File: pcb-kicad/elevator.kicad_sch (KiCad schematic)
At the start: 145 parts, among them SW1 MX-with-LED, SW10 MX-with-LED, SW11 MX-with-LED, SW12 MX-with-LED, SW13 MX-with-LED, SW14 MX-with-LED, SW15 MX-with-LED, SW16 MX-with-LED, SW17 MX-with-LED, SW18 MX-with-LED, SW19 MX-with-LED, SW2 MX-with-LED, SW20 MX-with-LED, SW21 MX-with-LED, SW22 MX-with-LED, SW23 MX-with-LED, SW24 MX-with-LED, SW25 MX-with-LED, SW26 MX-with-LED, SW27 MX-with-LED, SW28 MX-with-LED, SW29 MX-with-LED, SW3 MX-with-LED, SW30 MX-with-LED, SW31 MX-with-LED, SW32 MX-with-LED, SW33 MX-with-LED, SW34 MX-with-LED, SW35 MX-with-LED, SW36 MX-with-LED, SW37 MX-with-LED, SW38 MX-with-LED, SW39 MX-with-LED, SW4 MX-with-LED, SW40 MX-with-LED, SW41 MX-with-LED, SW42 MX-with-LED, SW43 MX-with-LED, SW44 MX-with-LED, SW45 MX-with-LED, SW46 MX-with-LED, SW47 MX-with-LED, SW48 MX-with-LED, SW5 MX-with-LED, SW6 MX-with-LED, SW7 MX-with-LED, SW8 MX-with-LED, SW9 MX-with-LED, U1 Frood

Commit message: Update schematic
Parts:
- added Q1: AO3416, Package_TO_SOT_SMD:SOT-23, symbol Transistor_FET:AO3400A
- added R49: R_LED_PWM, symbol Device:R_Small
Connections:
- net COL0: now also U1.26 (GPIO29)
- net COL1: now also U1.25 (GPIO28)
- net COL2: now also U1.24 (GPIO27)
- net COL3: now also U1.23 (GPIO26)
- net COL4: now also U1.22 (GPIO22)
- net COL5: now also U1.21 (GPIO20)
- net GND: now also U1.4 (GND), U1.5 (GND), Q1.2 (S)
- net LED_D: now also Q1.3 (D)
- net ROW0: now also U1.2 (GPIO0)
- net ROW1: now also U1.3 (GPIO1)
- net ROW2: now also U1.6 (GPIO2)
- net ROW3: now also U1.7 (GPIO3)
- net ROW4: now also U1.8 (GPIO4)
- net ROW5: now also U1.9 (GPIO5)
- net ROW6: now also U1.10 (GPIO6)
- net ROW7: now also U1.11 (GPIO7)
- net LED_PWM: now reaches U1.19 (GPIO21)
- net LED_PWM: now also R49.2
- new net: Q1.1 (G), R49.1
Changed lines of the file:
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@@
     (effects (font (size 1.27 1.27)) (justify right bottom))
   )
+  (label "LED_D" (at 58.42 33.02 180) (fields_autoplaced)
+    (effects (font (size 1.27 1.27)) (justify right bottom))
+  )
   (label "ROW6" (at 170.18 129.54 180) (fields_autoplaced)
     (effects (font (size 1.27 1.27)) (justify right bottom))
   )
+  (label "COL2" (at 104.14 100.33 0) (fields_autoplaced)
+    (effects (font (size 1.27 1.27)) (justify left bottom))
+  )
   (label "VCC" (at 350.52 121.92 180) (fields_autoplaced)
     (effects (font (size 1.27 1.27)) (justify right bottom))
   )
+  (label "LED_PWM" (at 63.5 45.72 270) (fields_autoplaced)
+    (effects (font (size 1.27 1.27)) (justify right bottom))
+  )
+  (label "COL5" (at 104.14 107.95 0) (fields_autoplaced)
+    (effects (font (size 1.27 1.27)) (justify left bottom))
+  )
   (label "VCC" (at 236.22 97.79 180) (fields_autoplaced)
     (effects (font (size 1.27 1.27)) (justify right bottom))
@@
     (effects (font (size 1.27 1.27)) (justify right bottom))
   )
+  (label "ROW1" (at 63.5 87.63 180) (fields_autoplaced)
+    (effects (font (size 1.27 1.27)) (justify right bottom))
+  )
   (label "VCC" (at 179.07 97.79 180) (fields_autoplaced)
     (effects (font (size 1.27 1.27)) (justify right bottom))
@@
     (effects (font (size 1.27 1.27)) (justify left bottom))
   )
+  (label "COL0" (at 104.14 95.25 0) (fields_autoplaced)
+    (effects (font (size 1.27 1.27)) (justify left bottom))
+  )
   (label "LED_D" (at 360.68 55.88 180) (fields_autoplaced)
     (effects (font (size 1.27 1.27)) (justify right bottom))
@@
     (effects (font (size 1.27 1.27)) (justify left bottom))
   )
+  (label "ROW6" (at 63.5 105.41 180) (fields_autoplaced)
+    (effects (font (size 1.27 1.27)) (justify right bottom))
+  )
   (label "VCC" (at 388.62 50.8 180) (fields_autoplaced)
     (effects (font (size 1.27 1.27)) (justify right bottom))
@@
     (effects (font (size 1.27 1.27)) (justify right bottom))
   )
+  (label "GND" (at 68.58 33.02 0) (fields_autoplaced)
+    (effects (font (size 1.27 1.27)) (justify left bottom))
+  )
+  (label "GND" (at 63.5 90.17 180) (fields_autoplaced)
+    (effects (font (size 1.27 1.27)) (justify right bottom))
+  )
   (label "VCC" (at 255.27 50.8 180) (fields_autoplaced)
     (effects (font (size 1.27 1.27)) (justify right bottom))
@@
     (effects (font (size 1.27 1.27)) (justify right bottom))
   )
+  (label "ROW4" (at 63.5 100.33 180) (fields_autoplaced)
+    (effects (font (size 1.27 1.27)) (justify right bottom))
+  )
   (label "VCC" (at 236.22 74.93 180) (fields_autoplaced)
     (effects (font (size 1.27 1.27)) (justify right bottom))
   )
+  (label "COL3" (at 104.14 102.87 0) (fields_autoplaced)
+    (effects (font (size 1.27 1.27)) (justify left bottom))
+  )
   (label "LED_D" (at 398.78 102.87 180) (fields_autoplaced)
     (effects (font (size 1.27 1.27)) (justify right bottom))
   )
+  (label "ROW5" (at 63.5 102.87 180) (fields_autoplaced)
+    (effects (font (size 1.27 1.27)) (justify right bottom))
+  )
   (label "LED_D" (at 303.53 127 180) (fields_autoplaced)
     (effects (font (size 1.27 1.27)) (justify right bottom))
@@
     (effects (font (size 1.27 1.27)) (justify right bottom))
   )
+  (label "ROW7" (at 63.5 107.95 180) (fields_autoplaced)
+    (effects (font (size 1.27 1.27)) (justify right bottom))
+  )
   (label "VCC" (at 350.52 50.8 180) (fields_autoplaced)
     (effects (font (size 1.27 1.27)) (justify right bottom))
@@
     (effects (font (size 1.27 1.27)) (justify right bottom))
   )
+  (label "ROW0" (at 63.5 85.09 180) (fields_autoplaced)
+    (effects (font (size 1.27 1.27)) (justify right bottom))
+  )
   (label "LED_D" (at 246.38 80.01 180) (fields_autoplaced)
     (effects (font (size 1.27 1.27)) (justify right bottom))
@@
     (effects (font (size 1.27 1.27)) (justify left bottom))
   )
+  (label "ROW2" (at 63.5 95.25 180) (fields_autoplaced)
+    (effects (font (size 1.27 1.27)) (justify right bottom))
+  )
   (label "LED_D" (at 227.33 127 180) (fields_autoplaced)
     (effects (font (size 1.27 1.27)) (justify right bottom))
@@
     (effects (font (size 1.27 1.27)) (justify right bottom))
   )
+  (label "COL1" (at 104.14 97.79 0) (fields_autoplaced)
+    (effects (font (size 1.27 1.27)) (justify left bottom))
+  )
   (label "VCC" (at 388.62 97.79 180) (fields_autoplaced)
     (effects (font (size 1.27 1.27)) (justify right bottom))
@@
     (effects (font (size 1.27 1.27)) (justify right bottom))
   )
+  (label "LED_PWM" (at 104.14 113.03 0) (fields_autoplaced)
+    (effects (font (size 1.27 1.27)) (justify left bottom))
+  )
   (label "VCC" (at 255.27 97.79 180) (fields_autoplaced)
     (effects (font (size 1.27 1.27)) (justify right bottom))
@@
     (effects (font (size 1.27 1.27)) (justify right bottom))
   )
+  (label "ROW3" (at 63.5 97.79 180) (fields_autoplaced)
+    (effects (font (size 1.27 1.27)) (justify right bottom))
+  )
   (label "VCC" (at 179.07 74.93 180) (fields_autoplaced)
     (effects (font (size 1.27 1.27)) (justify right bottom))
@@
     (effects (font (size 1.27 1.27)) (justify right bottom))
   )
+  (label "GND" (at 63.5 92.71 180) (fields_autoplaced)
+    (effects (font (size 1.27 1.27)) (justify right bottom))
+  )
   (label "VCC" (at 331.47 121.92 180) (fields_autoplaced)
     (effects (font (size 1.27 1.27)) (justify right bottom))
@@
     (effects (font (size 1.27 1.27)) (justify right bottom))
   )
+  (label "COL4" (at 104.14 105.41 0) (fields_autoplaced)
+    (effects (font (size 1.27 1.27)) (justify left bottom))
+  )
   (label "VCC" (at 179.07 50.8 180) (fields_autoplaced)
     (effects (font (size 1.27 1.27)) (justify right bottom))
@@
     )
   )
+  (symbol (lib_id "Device:R_Small") (at 63.5 43.18 0) (unit 1)
+    (in_bom yes) (on_board yes) (dnp no) (fields_autoplaced)
+    (property "Reference" "R49" (at 66.04 41.91 0)
+      (effects (font (size 1.27 1.27)) (justify left))
+    )
+    (property "Value" "R_LED_PWM" (at 66.04 44.45 0)
+      (effects (font (size 1.27 1.27)) (justify left))
+    )
+    (property "Footprint" "" (at 63.5 43.18 0)
+      (effects (font (size 1.27 1.27)) hide)
+    )
+    (property "Datasheet" "~" (at 63.5 43.18 0)
+      (effects (font (size 1.27 1.27)) hide)
+    )
+    (pin "1")
+    (pin "2")
+    (instances
+      (project "elevator"
+        (path "/ec52aef2-1869-4a70-a72a-c2d0a3ee9ccf"
+          (reference "R49") (unit 1)
+        )
+      )
+    )
+  )
   (symbol (lib_id "Device:R_Small") (at 322.58 77.47 180) (unit 1)
     (in_bom yes) (on_board yes) (dnp no)
@@
         )
       )
+    )
+  )
+  (symbol (lib_id "Transistor_FET:AO3400A") (at 63.5 35.56 90) (unit 1)
+    (in_bom yes) (on_board yes) (dnp no) (fields_autoplaced)
+    (property "Reference" "Q1" (at 63.5 26.67 90)
+      (effects (font (size 1.27 1.27)))
+    )
+    (property "Value" "AO3416" (at 63.5 29.21 90)
+      (effects (font (size 1.27 1.27)))
+    )
+    (property "Footprint" "Package_TO_SOT_SMD:SOT-23" (at 65.405 30.48 0)
+      (effects (font (size 1.27 1.27) italic) (justify left) hide)
+    )
+    (property "Datasheet" "http://www.aosmd.com/pdfs/datasheet/AO3400A.pdf" (at 67.31 30.48 0)
+      (effects (font (size 1.27 1.27)) (justify left) hide)
+    )
+    (pin "1")
+    (pin "3")
+    (pin "2")
+    (instances
+      (project "elevator"
+        (path "/ec52aef2-1869-4a70-a72a-c2d0a3ee9ccf"
+          (reference "Q1") (unit 1)
+        )
+      )

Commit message: Change schematic a bit and update PCB
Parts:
- D1, D10, D11, D12, D13, D14, D15, D16, D17, D18, D19, D2, D20, D21, D22, D23, D24, D25, D26, D27, D28, D29, D3, D30, D31, D32, D33, D34, D35, D36, D37, D38, D39, D4, D40, D41, D42, D43, D44, D45, D46, D47, D48, D5, D6, D7, D8, D9: value D_LED -> D_SW; footprint (none) -> Keebio-Parts:Diode-dual
- R1, R10, R11, R12, R13, R14, R15, R16, R17, R18, R19, R2, R20, R21, R22, R23, R24, R25, R26, R27, R28, R29, R3, R30, R31, R32, R33, R34, R35, R36, R37, R38, R39, R4, R40, R41, R42, R43, R44, R45, R46, R47, R48, R49, R5, R6, R7, R8, R9: footprint (none) -> Keebio-Parts:Resistor-Hybrid
- SW1, SW10, SW11, SW12, SW13, SW14, SW15, SW16, SW17, SW18, SW19, SW2, SW20, SW21, SW22, SW23, SW24, SW25, SW26, SW27, SW28, SW29, SW3, SW30, SW31, SW32, SW33, SW34, SW35, SW36, SW37, SW38, SW39, SW4, SW40, SW41, SW42, SW43, SW44, SW45, SW46, SW47, SW48, SW5, SW6, SW7, SW8, SW9: footprint (none) -> Keebio-Parts:MX-Alps-Choc-1U
- U1: footprint 42keebs:Frood_PinHeader_2x13+5_P2.54mm_Labels_Top -> footprints:Frood_PinHeader_2x13+5_P2.54mm_Labels_Top

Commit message: Minor changes
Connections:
- net ROW0: now also U1.20 (GPIO23); no longer U1.2 (GPIO0)
- net ROW1: now also U1.13 (GPIO9); no longer U1.3 (GPIO1)
- net ROW2: now also U1.12 (GPIO8); no longer U1.6 (GPIO2)
- net ROW3: now also U1.11 (GPIO7); no longer U1.7 (GPIO3)
- net ROW4: now also U1.10 (GPIO6); no longer U1.8 (GPIO4)
- net ROW5: now also U1.8 (GPIO4); no longer U1.9 (GPIO5)
- net ROW6: now also U1.3 (GPIO1); no longer U1.10 (GPIO6)
- net ROW7: now also U1.2 (GPIO0); no longer U1.11 (GPIO7)
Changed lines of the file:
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@@
     (effects (font (size 1.27 1.27)) (justify right bottom))
   )
-  (label "ROW1" (at 63.5 87.63 180) (fields_autoplaced)
+  (label "ROW1" (at 63.5 113.03 180) (fields_autoplaced)
     (effects (font (size 1.27 1.27)) (justify right bottom))
   )
@@
     (effects (font (size 1.27 1.27)) (justify left bottom))
   )
-  (label "ROW6" (at 63.5 105.41 180) (fields_autoplaced)
+  (label "ROW6" (at 63.5 87.63 180) (fields_autoplaced)
     (effects (font (size 1.27 1.27)) (justify right bottom))
   )
@@
     (effects (font (size 1.27 1.27)) (justify right bottom))
   )
-  (label "ROW4" (at 63.5 100.33 180) (fields_autoplaced)
+  (label "ROW4" (at 63.5 105.41 180) (fields_autoplaced)
     (effects (font (size 1.27 1.27)) (justify right bottom))
   )
@@
     (effects (font (size 1.27 1.27)) (justify right bottom))
   )
-  (label "ROW5" (at 63.5 102.87 180) (fields_autoplaced)
+  (label "ROW5" (at 63.5 100.33 180) (fields_autoplaced)
     (effects (font (size 1.27 1.27)) (justify right bottom))
   )
@@
     (effects (font (size 1.27 1.27)) (justify right bottom))
   )
-  (label "ROW7" (at 63.5 107.95 180) (fields_autoplaced)
+  (label "ROW7" (at 63.5 85.09 180) (fields_autoplaced)
     (effects (font (size 1.27 1.27)) (justify right bottom))
   )
@@
     (effects (font (size 1.27 1.27)) (justify right bottom))
   )
-  (label "ROW0" (at 63.5 85.09 180) (fields_autoplaced)
-    (effects (font (size 1.27 1.27)) (justify right bottom))
+  (label "ROW0" (at 104.14 110.49 0) (fields_autoplaced)
+    (effects (font (size 1.27 1.27)) (justify left bottom))
   )
   (label "LED_D" (at 246.38 80.01 180) (fields_autoplaced)
@@
     (effects (font (size 1.27 1.27)) (justify left bottom))
   )
-  (label "ROW2" (at 63.5 95.25 180) (fields_autoplaced)
+  (label "ROW2" (at 63.5 110.49 180) (fields_autoplaced)
     (effects (font (size 1.27 1.27)) (justify right bottom))
   )
@@
     (effects (font (size 1.27 1.27)) (justify right bottom))
   )
-  (label "ROW3" (at 63.5 97.79 180) (fields_autoplaced)
-    (effects (font (size 1.27 1.27)) (justify right bottom))
-  )
+  (label "ROW3" (at 63.5 107.95 180) (fields_autoplaced)
+    (effects (font (size 1.27 1.27)) (justify right bottom))
+  )

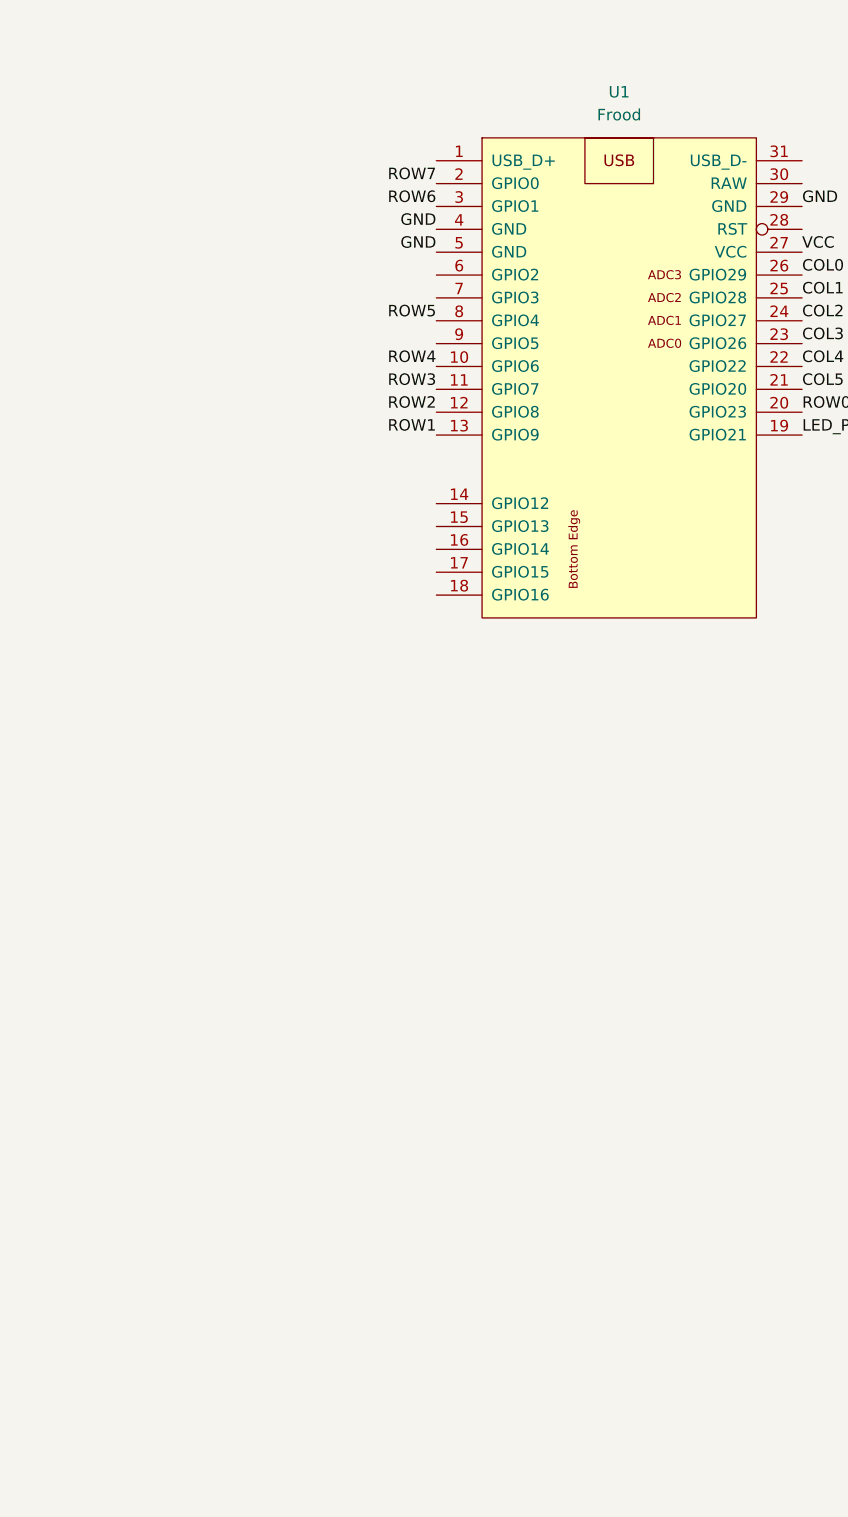
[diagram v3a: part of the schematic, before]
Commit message: Finish matrix wiring, add encoder schematic
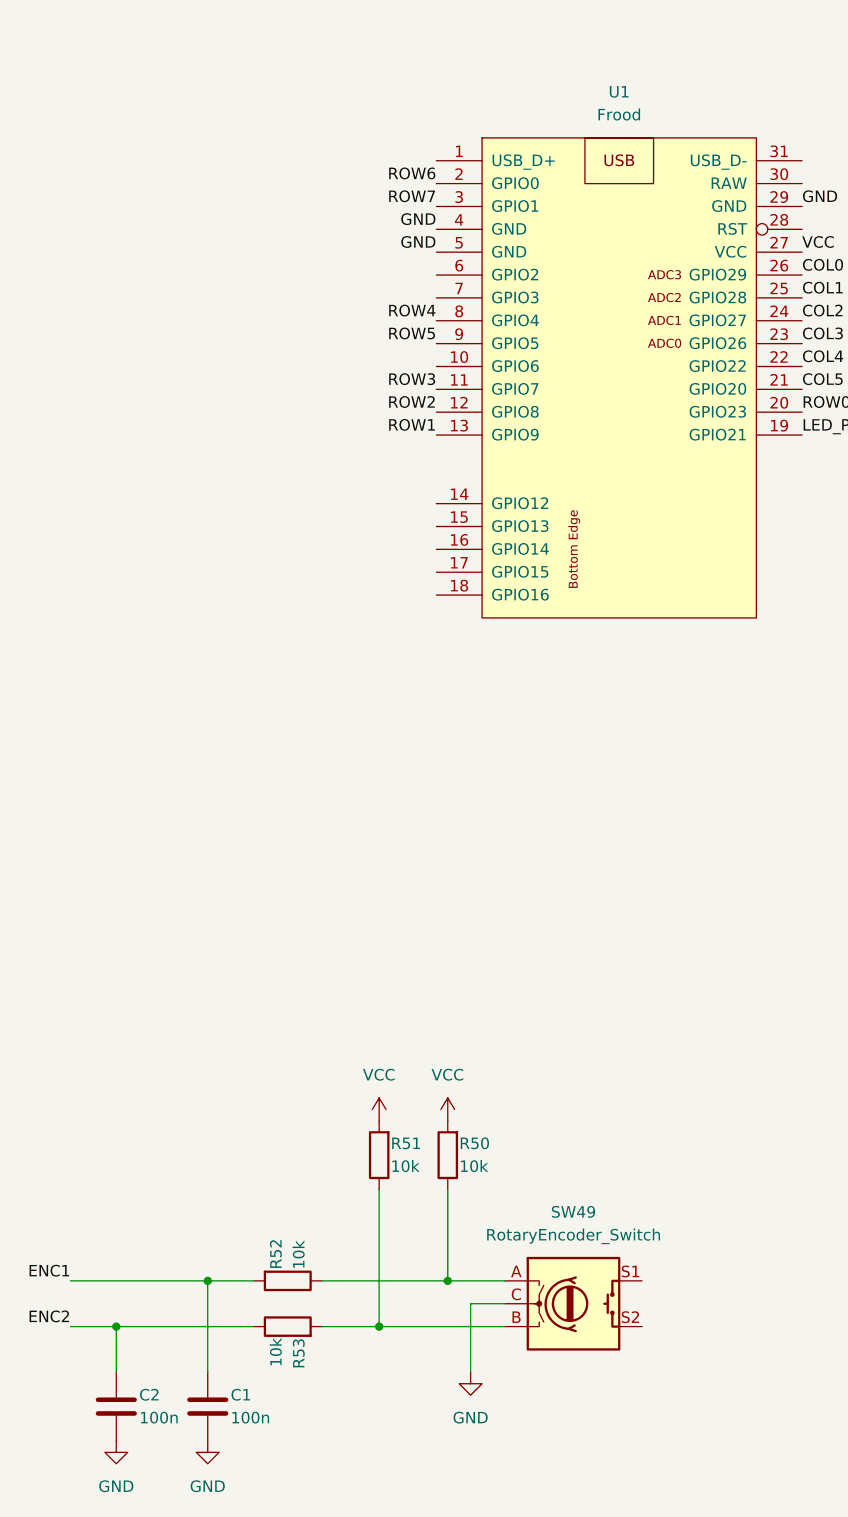
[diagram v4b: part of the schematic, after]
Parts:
- added C1, C2: 100n, symbol Device:C
- added R50, R51, R52, R53: 10k, symbol Device:R
- added SW49: RotaryEncoder_Switch, symbol Device:RotaryEncoder_Switch
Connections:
- net GND: now also C1.2, C2.2, SW49.C
- net ROW4: now also U1.8 (GPIO4); no longer U1.10 (GPIO6)
- net ROW5: now also U1.9 (GPIO5); no longer U1.8 (GPIO4)
- net ROW6: now also U1.2 (GPIO0); no longer U1.3 (GPIO1)
- net ROW7: now also U1.3 (GPIO1); no longer U1.2 (GPIO0)
- net VCC: now also R50.2, R51.2
- new net: R50.1, R52.1, SW49.A
- new net: R51.1, R53.2, SW49.B
- new net ENC1: C1.1, R52.2
- new net ENC2: C2.1, R53.1
